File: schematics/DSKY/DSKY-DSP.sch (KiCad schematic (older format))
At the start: 0 parts

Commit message: Final tweaks, the DSKY is now complete!
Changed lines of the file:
@@
 	3950 4050 3800 4050
 Text HLabel 5600 2850 0    50   Input ~ 0
-CLK2
+CLK3
 $Sheet
 S 1850 2950 1100 1200
@@
 	5000 2500 5150 2500
 Wire Bus Line
-	7200 4350 8450 4350
+	7200 4450 8450 4450
 Wire Bus Line
 	2950 3250 3550 3250
@@
 INDC
 Wire Bus Line
-	7200 4500 8450 4500
+	7200 4550 8450 4550
 Connection ~ 3550 3250
 Wire Bus Line
 	3550 3250 3550 3600
 Wire Wire Line
-	7200 4850 8450 4850
+	7200 4750 8450 4750
 Wire Bus Line
 	7200 2600 8450 2600
@@
 	7200 2450 8450 2450
 Wire Bus Line
-	7200 3500 7550 3500
-Wire Bus Line
-	7550 4150 7200 4150
+	7200 3300 7600 3300
+Wire Bus Line
+	7600 4350 7200 4350
 Wire Bus Line
 	5000 3600 5850 3600
@@
 	3550 3250 5500 3250
 Wire Bus Line
-	5500 3250 5500 5650
+	5500 3250 5500 5750
 Connection ~ 5500 3250
 Wire Bus Line
@@
 	5850 4450 5450 4450
 Text HLabel 5450 4450 0    50   Input ~ 0
-CLK2
+CLK3
 Wire Bus Line
 	5150 4300 5850 4300
@@
 F0 "DSKY_DSP_LCD" 50
 F1 "DSKY_DSP_LCD.sch" 50
-F2 "DA1[1..3]" I L 8450 4350 50
+F2 "DA1[1..3]" I L 8450 4450 50
 F3 "ID2[0..3]" I L 8450 2150 50
-F4 "WRITE1" I L 8450 4850 50
+F4 "WRITE1" I L 8450 4750 50
 F5 "WRITE2" I L 8450 3050 50
 F6 "WRITE3" I L 8450 3150 50
-F7 "ID1[0..3]" I L 8450 4500 50
+F7 "ID1[0..3]" I L 8450 4550 50
 F8 "ID3[0..3]" I L 8450 2300 50
 F9 "DA2[1..3]" I L 8450 2450 50
@@
 F2 "OW[12..15]" I L 5850 3250 50
 F3 "DISP" I L 5850 2750 50
-F4 "CLK2" I L 5850 2850 50
+F4 "CLK3" I L 5850 2850 50
 F5 "RWD[12..12]" O L 5850 3600 50
 F6 "DA2[1..3]" O R 7200 2450 50
@@
 F8 "WRITE2" O R 7200 3050 50
 F9 "WRITE3" O R 7200 3150 50
-F10 "RWD[1..11]" O R 7200 3500 50
+F10 "RWD[1..11]" O R 7200 3300 50
 F11 "MODE1" O R 7200 2750 50
 F12 "MODE2" O R 7200 2850 50
 F13 "MODE3" O R 7200 2950 50
+F14 "INDC" I L 5850 2650 50
+F15 "COMB-A" O R 7200 3400 50
+F16 "COMB-B" O R 7200 3500 50
+F17 "COMB-C" O R 7200 3600 50
 $EndSheet
 Text HLabel 3800 4350 0    50   Input ~ 0
@@
 CLK2
 Wire Bus Line
-	5500 5650 5850 5650
+	5500 5750 5850 5750
 Wire Bus Line
 	8450 4650 7700 4650
-Wire Bus Line
-	7700 4650 7700 6100
-Text HLabel 5700 5850 0    50   Input ~ 0
+Text HLabel 5700 5950 0    50   Input ~ 0
 DSKYRST
 Wire Wire Line
-	5700 5850 5850 5850
-Wire Bus Line
-	7550 3500 7550 4150
-Connection ~ 7550 4150
-Wire Bus Line
-	7550 4150 7550 5950
-Wire Bus Line
-	7550 5950 7200 5950
-Wire Bus Line
-	7700 6100 7200 6100
-Wire Wire Line
-	7200 5150 7300 5150
-Wire Wire Line
-	7300 5150 7300 5650
-Wire Wire Line
-	7300 5650 7200 5650
-Wire Wire Line
-	7200 5800 7450 5800
-Wire Wire Line
-	7450 5800 7450 5000
-Wire Wire Line
-	7450 5000 7200 5000
-$Sheet
-S 5850 3950 1350 1300
+	5700 5950 5850 5950
+Wire Bus Line
+	7600 6350 7200 6350
+Wire Bus Line
+	7700 6450 7200 6450
+$Sheet
+S 5850 3950 1350 1500
 U 64844A8A
 F0 "DSKY_DSP_DCD1" 50
 F1 "DSKY_DSP_DCD1.sch" 50
-F2 "DA1[1..3]" O R 7200 4350 50
-F3 "ID1[0..3]" O R 7200 4500 50
-F4 "WRITE1" O R 7200 4850 50
-F5 "RWD[1..11]" I R 7200 4150 50
+F2 "DA1[1..3]" O R 7200 4450 50
+F3 "ID1[0..3]" O R 7200 4550 50
+F4 "WRITE1" O R 7200 4750 50
+F5 "RWD[1..11]" I R 7200 4350 50
 F6 "ID3[0..3]" I L 5850 4300 50
-F7 "CLK2" I L 5850 4450 50
+F7 "CLK3" I L 5850 4450 50
 F8 "ID2[0..3]" I L 5850 4200 50
-F9 "DSPMINUS" I R 7200 5000 50
-F10 "DSPBLANK" I R 7200 5150 50
-$EndSheet
-$Sheet
-S 5850 5550 1350 850
+F9 "DSPMINUS" I R 7200 5250 50
+F10 "DSPBLANK" I R 7200 5350 50
+F11 "COMB-C" I R 7200 4000 50
+F12 "COMB-B" I R 7200 4100 50
+F13 "COMB-A" I R 7200 4200 50
+F14 "NRWD1" I R 7200 4850 50
+F15 "NRWD2" I R 7200 4950 50
+F16 "NRWD4" I R 7200 5050 50
+F17 "NRWD5" I R 7200 5150 50
+$EndSheet
+Wire Wire Line
+	5850 6050 5700 6050
+Text HLabel 5700 6050 0    50   Input ~ 0
+SGN_CLK2
+Wire Wire Line
+	5850 2650 5600 2650
+Text HLabel 5600 2650 0    50   Input ~ 0
+INDC
+Wire Bus Line
+	7700 4650 7700 6450
+Connection ~ 7600 4350
+Wire Bus Line
+	7600 4350 7600 6350
+Wire Bus Line
+	7600 3300 7600 4350
+Wire Wire Line
+	7200 3600 7250 3600
+Wire Wire Line
+	7250 3600 7250 4000
+Wire Wire Line
+	7250 4000 7200 4000
+Wire Wire Line
+	7200 3500 7350 3500
+Wire Wire Line
+	7350 3500 7350 4100
+Wire Wire Line
+	7350 4100 7200 4100
+Wire Wire Line
+	7200 3400 7450 3400
+Wire Wire Line
+	7450 3400 7450 4200
+Wire Wire Line
+	7450 4200 7200 4200
+Connection ~ 5500 5750
+Wire Bus Line
+	5500 5750 5500 5900
+$Sheet
+S 5850 5650 1350 900
 U 61C9EF7C
 F0 "DSKY-DSP-SIGN" 50
 F1 "DSKY-DSP-SIGN.sch" 50
-F2 "OW[11..11]" I L 5850 5650 50
-F3 "ID1[4..4]" O R 7200 6100 50
-F4 "RWD[1..7]" I R 7200 5950 50
-F5 "DSKYRST" I L 5850 5850 50
-F6 "DSPBLANK" O R 7200 5650 50
-F7 "DSPMINUS" O R 7200 5800 50
-F8 "SGN_CLK2" I L 5850 5950 50
-$EndSheet
-Wire Wire Line
-	5850 5950 5700 5950
-Text HLabel 5700 5950 0    50   Input ~ 0
-SGN_CLK2
+F2 "OW[11..11]" I L 5850 5750 50
+F3 "ID1[4..4]" O R 7200 6450 50
+F4 "RWD[1..7]" I R 7200 6350 50
+F5 "DSKYRST" I L 5850 5950 50
+F6 "DSPBLANK" O R 7200 5750 50
+F7 "DSPMINUS" O R 7200 5850 50
+F8 "SGN_CLK2" I L 5850 6050 50
+F9 "NRWD5" O R 7200 5950 50
+F10 "NRWD4" O R 7200 6050 50
+F11 "NRWD2" O R 7200 6150 50
+F12 "NRWD1" O R 7200 6250 50
+$EndSheet
+Wire Wire Line
+	7200 5350 7250 5350
+Wire Wire Line
+	7250 5350 7250 5750
+Wire Wire Line
+	7250 5750 7200 5750
+Wire Wire Line
+	7200 5250 7300 5250
+Wire Wire Line
+	7300 5250 7300 5850
+Wire Wire Line
+	7300 5850 7200 5850
+Wire Wire Line
+	7200 5150 7350 5150
+Wire Wire Line
+	7350 5150 7350 5950
+Wire Wire Line
+	7350 5950 7200 5950
+Wire Wire Line
+	7200 5050 7400 5050
+Wire Wire Line
+	7400 5050 7400 6050
+Wire Wire Line
+	7400 6050 7200 6050
+Wire Wire Line
+	7200 4950 7450 4950
+Wire Wire Line
+	7450 4950 7450 6150
+Wire Wire Line
+	7450 6150 7200 6150
+Wire Wire Line
+	7200 4850 7500 4850
+Wire Wire Line
+	7500 4850 7500 6250
+Wire Wire Line
+	7500 6250 7200 6250
 $EndSCHEMATC

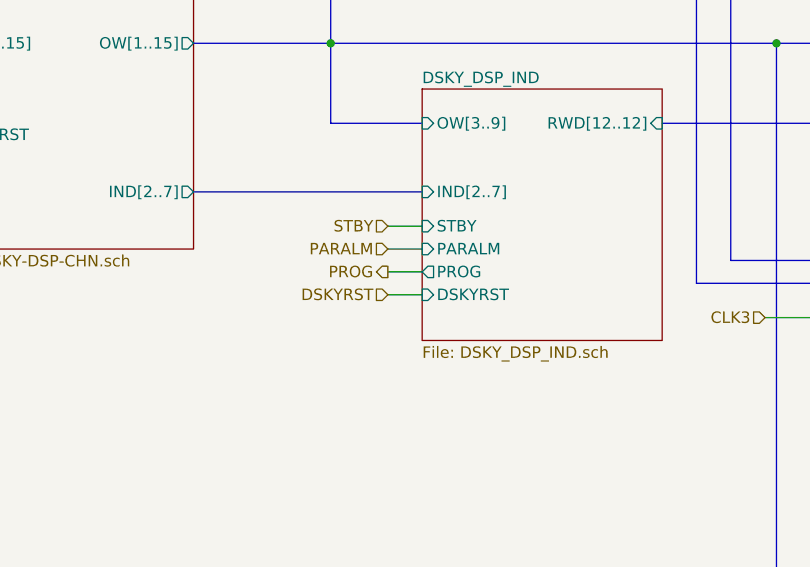
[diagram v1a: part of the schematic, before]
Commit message: Added DSKY test schematic
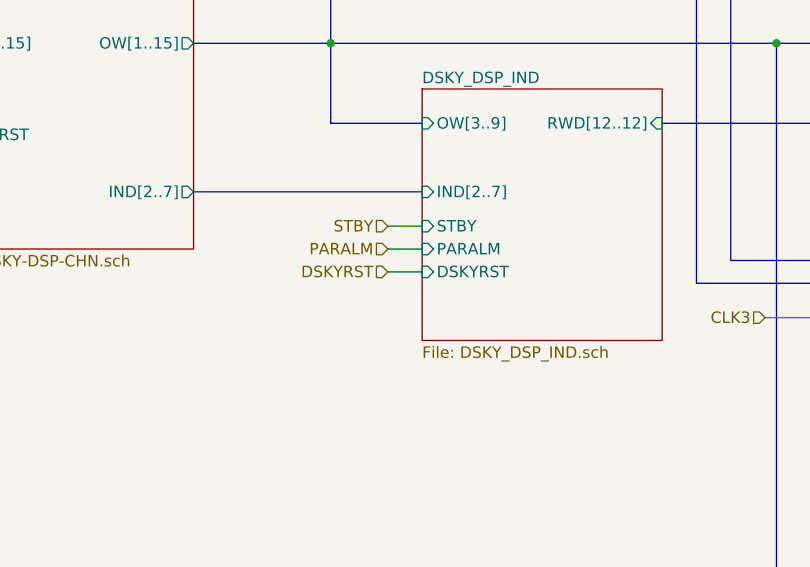
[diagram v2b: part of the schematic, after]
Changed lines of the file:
@@
 $Descr A 11000 8500
 encoding utf-8
-Sheet 2 11
+Sheet 2 12
 Title ""
 Date ""
@@
 F5 "PARALM" I L 3950 4150 50
 F6 "IND[2..7]" I L 3950 3900 50
-F7 "PROG" O L 3950 4250 50
-F8 "DSKYRST" I L 3950 4350 50
+F7 "DSKYRST" I L 3950 4250 50
 $EndSheet
 Wire Bus Line
@@
 Wire Wire Line
 	3950 4250 3800 4250
-Text HLabel 3800 4250 0    50   Output ~ 0
-PROG
 Wire Wire Line
 	7200 2750 8450 2750
@@
 F17 "COMB-C" O R 7200 3600 50
 $EndSheet
-Text HLabel 3800 4350 0    50   Input ~ 0
+Text HLabel 3800 4250 0    50   Input ~ 0
 DSKYRST
 Wire Wire Line
-	3800 4350 3950 4350
-Wire Wire Line
 	1850 3550 1600 3550

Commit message: Minor DSKY tweaks.
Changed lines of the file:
@@
 $Descr A 11000 8500
 encoding utf-8
-Sheet 5 15
+Sheet 4 15
 Title ""
 Date ""
@@
 F8 "DE[2..3]" O L 6250 4750 50
 F9 "IND[6..6]" I L 6250 5350 50
-F10 "DSKYRST" I L 6250 5500 50
+F10 "SGNRST" I L 6250 5500 50
 $EndSheet
 $Sheet
@@
 	6250 5500 6100 5500
 Text HLabel 6100 5500 0    50   Input ~ 0
-DSKYRST
+SGNRST
 $EndSCHEMATC

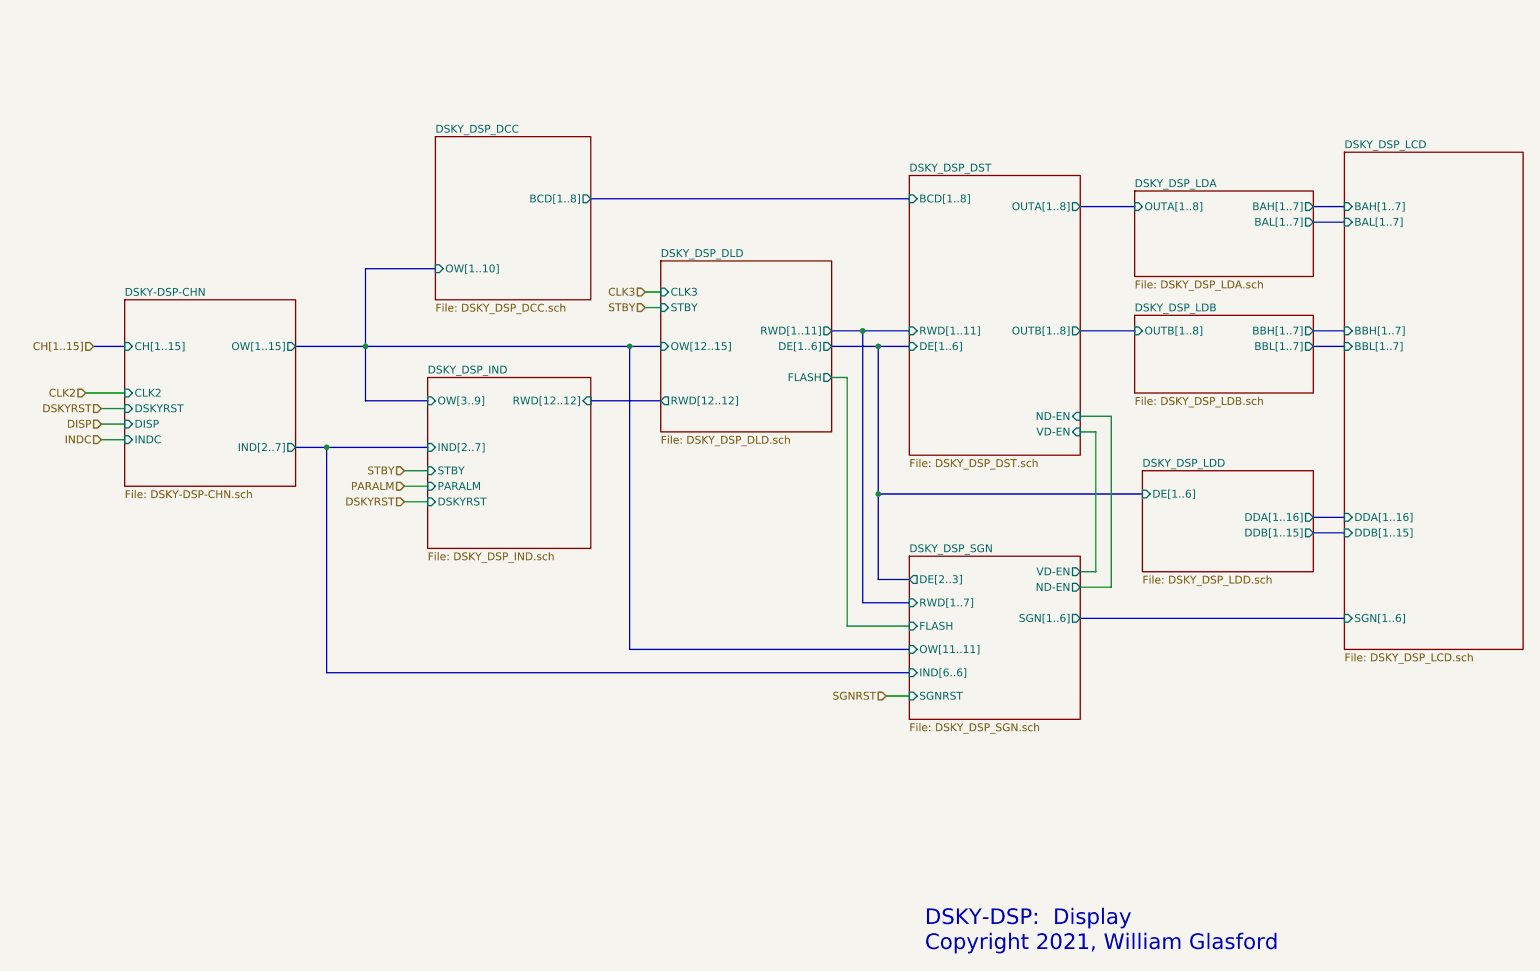
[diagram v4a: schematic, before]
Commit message: Using 4 LED driver chips.
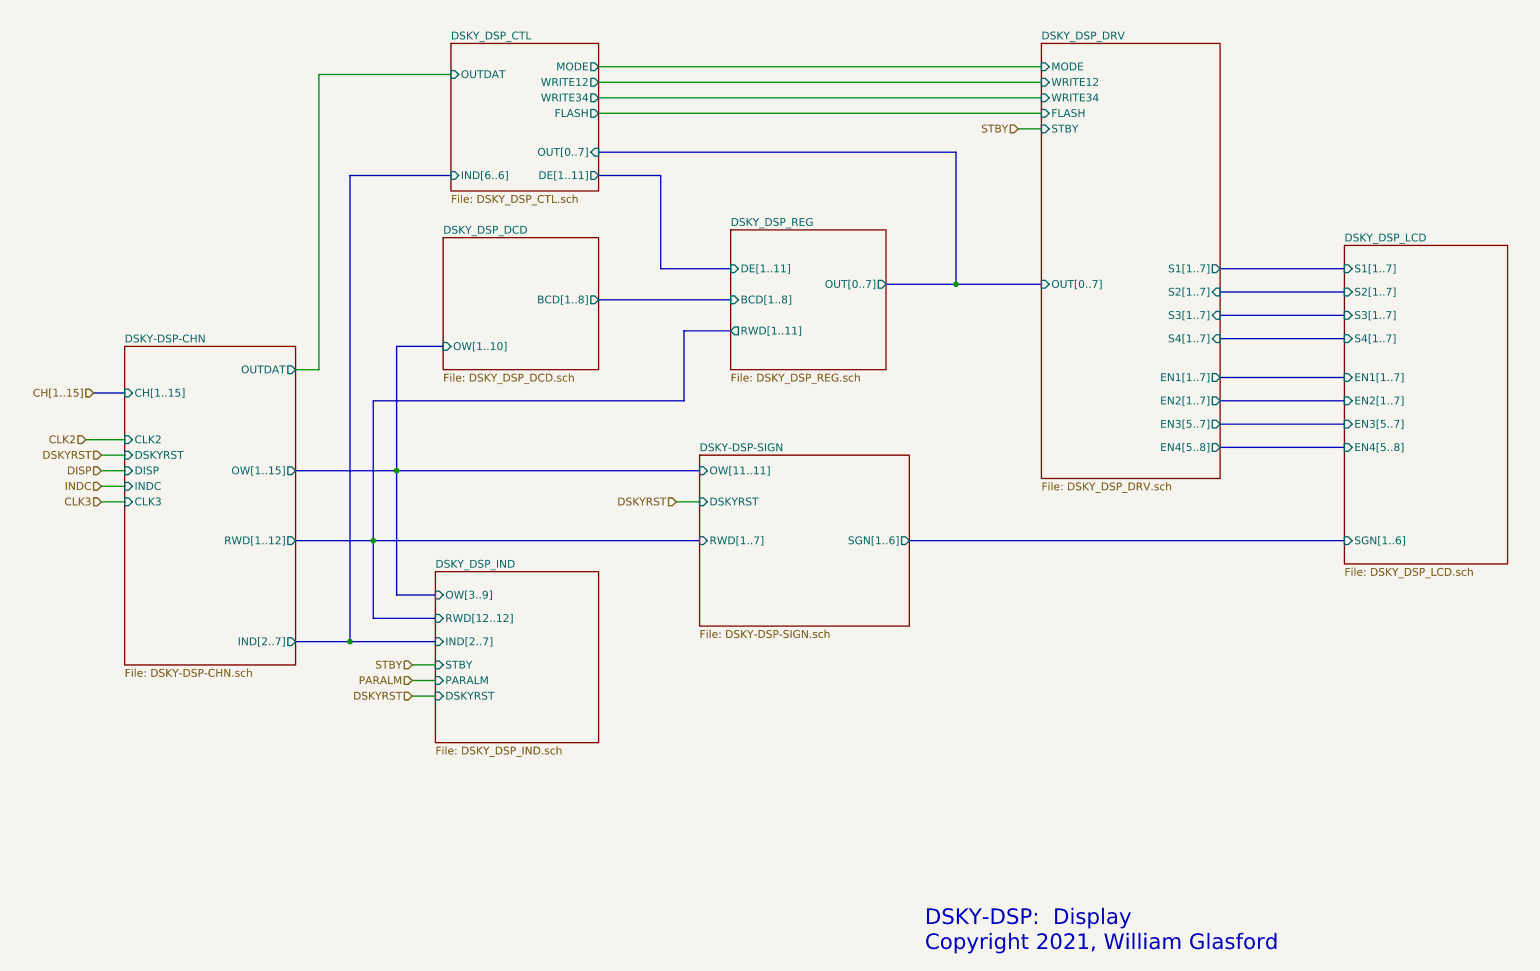
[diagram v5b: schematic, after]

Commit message: Modified to use fourth display decoder chip.
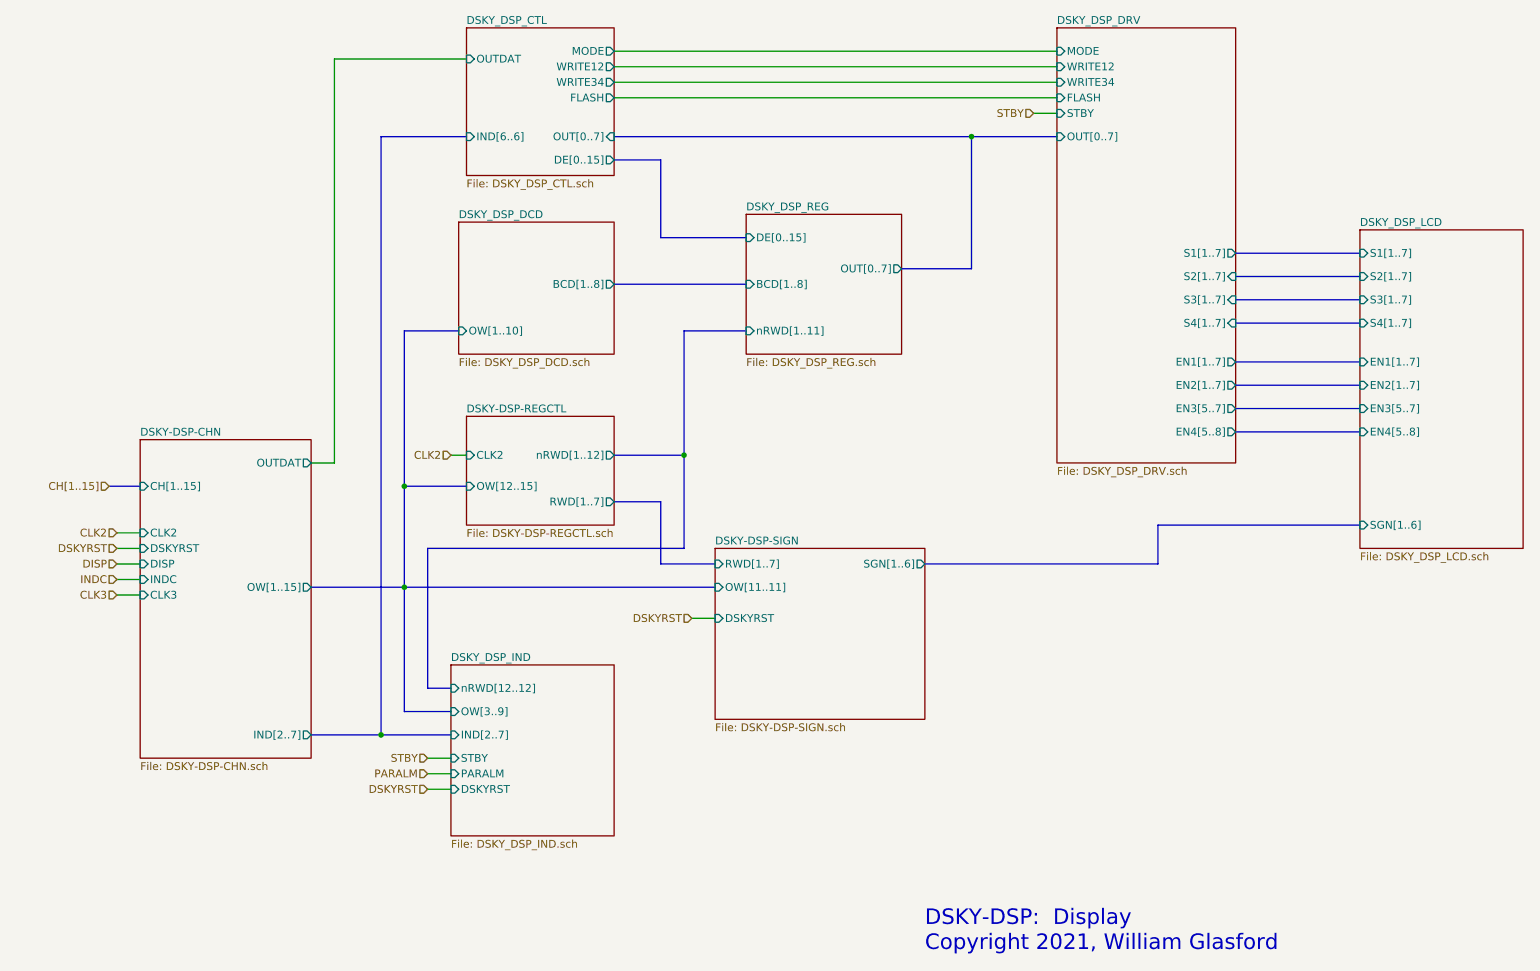
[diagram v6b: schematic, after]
